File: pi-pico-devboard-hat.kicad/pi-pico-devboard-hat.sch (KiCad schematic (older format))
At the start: 27 parts, among them J1 Conn_01x24_Male, J2 I2C, J3 SDA_UP, J4 SCL_UP, J5 Conn_SPI, J6 Conn_Ext, J7 Conn_BTN, J8 Conn_LED, P1 Conn_02x20_Odd_Even, SW1 SW_Reset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

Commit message: Rev 8: added power-connector / fine-tuning
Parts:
- added J9: Conn_02x03_Odd_Even, Connector_PinHeader_2.54mm:PinHeader_2x03_P2.54mm_Vertical, symbol Connector_Generic:Conn_02x03_Odd_Even
- J5: footprint Connector_PinHeader_2.54mm:PinHeader_1x07_P2.54mm_Vertical -> Connector_PinHeader_2.54mm:PinHeader_1x06_P2.54mm_Vertical; symbol Connector:Conn_01x07_Male -> Connector:Conn_01x06_Male
- J6: footprint Connector_PinHeader_2.54mm:PinHeader_1x04_P2.54mm_Vertical -> Connector_PinHeader_2.54mm:PinHeader_1x03_P2.54mm_Vertical; symbol Connector:Conn_01x04_Male -> Connector:Conn_01x03_Male
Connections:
- net 3V3: now also J9.1 (Pin_1), J9.3 (Pin_3), J9.5 (Pin_5)
- net GND: now also J9.2 (Pin_2), J9.4 (Pin_4), J9.6 (Pin_6)
- net GP8: now reaches U1.11 (GPIO8)
- net GP8: now also J6.3 (Pin_3)
- net SPI_CS_GP13: now reaches U1.17 (GPIO13)
- net SPI_CS_GP13: now also J5.6 (Pin_6)
- no-connect marks 23 -> 21
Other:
- note added: "Power"
- note removed: "SPI1_CS"
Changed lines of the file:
@@
 Title "pi-pico-devboard-hat"
 Date "2021-03-23"
-Rev "7"
+Rev "8"
 Comp "Bernhard Bablok"
 Comment1 "https://github.com/bablokb/pi-pico-devboard-hat"
@@
 NoConn ~ 6500 4200
 NoConn ~ 6500 4300
-NoConn ~ 6500 4400
 NoConn ~ 6500 4500
 NoConn ~ 6500 4700
 NoConn ~ 6500 4800
-NoConn ~ 6500 5000
 NoConn ~ 8700 4000
 NoConn ~ 8700 4200
@@
 Connection ~ 1350 4700
 $Comp
-L Connector:Conn_01x07_Male J5
+L Connector:Conn_01x06_Male J5
 U 1 1 605903A9
-P 950 5650
-F 0 "J5" H 1050 6200 50  0000 C CNN
-F 1 "Conn_SPI" H 1050 6100 50  0000 C CNN
-F 2 "Connector_PinHeader_2.54mm:PinHeader_1x07_P2.54mm_Vertical" H 950 5650 50  0001 C CNN
-F 3 "~" H 950 5650 50  0001 C CNN
-	1    950  5650
+P 950 5550
+F 0 "J5" H 1050 6000 50  0000 C CNN
+F 1 "Conn_SPI" H 1050 5900 50  0000 C CNN
+F 2 "Connector_PinHeader_2.54mm:PinHeader_1x06_P2.54mm_Vertical" H 950 5550 50  0001 C CNN
+F 3 "~" H 950 5550 50  0001 C CNN
+	1    950  5550
 	1    0    0    -1
 $EndComp
@@
 Wire Wire Line
 	1150 5750 1500 5750
-Wire Wire Line
-	1150 5950 1150 5850
-Text Notes 1250 5900 0    50   ~ 0
-SPI1_CS
 Text Label 6500 5300 2    50   ~ 0
 SPI1TX_GP15
@@
 Wire Notes Line
 	2600 3550 750  3550
-Wire Notes Line
-	750  6100 750  5000
 Text Notes 2000 4850 0    50   ~ 0
 I2C-Connector
@@
 SPI-Connector
 Wire Notes Line
-	2600 5000 2600 6100
-Wire Notes Line
 	750  5000 2600 5000
-Wire Notes Line
-	750  6100 2600 6100
-$Comp
-L Connector:Conn_01x04_Male J6
+$Comp
+L Connector:Conn_01x03_Male J6
 U 1 1 605A6142
 P 2850 5450
 F 0 "J6" H 2950 5800 50  0000 C CNN
 F 1 "Conn_Ext" H 2950 5700 50  0000 C CNN
-F 2 "Connector_PinHeader_2.54mm:PinHeader_1x04_P2.54mm_Vertical" H 2850 5450 50  0001 C CNN
+F 2 "Connector_PinHeader_2.54mm:PinHeader_1x03_P2.54mm_Vertical" H 2850 5450 50  0001 C CNN
 F 3 "~" H 2850 5450 50  0001 C CNN
 	1    2850 5450
@@
 Wire Wire Line
 	3050 5450 3700 5450
-Wire Wire Line
-	3050 5650 3050 5550
 Wire Notes Line
 	2750 5000 3800 5000
@@
 Text Notes 9450 2100 0    50   ~ 0
 LEDs
+Text Label 6500 5000 2    50   ~ 0
+SPI_CS_GP13
+Text Label 1500 5850 0    50   ~ 0
+SPI_CS_GP13
+Wire Wire Line
+	1150 5850 1500 5850
+Wire Notes Line
+	2600 5000 2600 6100
+Wire Notes Line
+	2600 6100 750  6100
+Wire Notes Line
+	750  6100 750  5000
+Text Label 6500 4400 2    50   ~ 0
+GP8
+Text Label 3400 5550 0    50   ~ 0
+GP8
+Wire Wire Line
+	3050 5550 3400 5550
+$Comp
+L Connector_Generic:Conn_02x03_Odd_Even J9
+U 1 1 608162C5
+P 3200 4000
+F 0 "J9" H 3250 4317 50  0000 C CNN
+F 1 "Conn_02x03_Odd_Even" H 3250 4226 50  0000 C CNN
+F 2 "Connector_PinHeader_2.54mm:PinHeader_2x03_P2.54mm_Vertical" H 3200 4000 50  0001 C CNN
+F 3 "~" H 3200 4000 50  0001 C CNN
+	1    3200 4000
+	1    0    0    -1
+$EndComp
+$Comp
+L power:GND #PWR011
+U 1 1 60817D38
+P 3500 4450
+F 0 "#PWR011" H 3500 4200 50  0001 C CNN
+F 1 "GND" V 3505 4322 50  0000 R CNN
+F 2 "" H 3500 4450 50  0001 C CNN
+F 3 "" H 3500 4450 50  0001 C CNN
+	1    3500 4450
+	1    0    0    -1
+$EndComp
+Text Label 3000 4500 3    50   ~ 0
+3V3
+Wire Wire Line
+	3000 4500 3000 4100
+Connection ~ 3000 4000
+Wire Wire Line
+	3000 4000 3000 3900
+Connection ~ 3000 4100
+Wire Wire Line
+	3000 4100 3000 4000
+Wire Wire Line
+	3500 4450 3500 4100
+Connection ~ 3500 4000
+Wire Wire Line
+	3500 4000 3500 3900
+Connection ~ 3500 4100
+Wire Wire Line
+	3500 4100 3500 4000
+Wire Notes Line
+	3800 4900 3800 3550
+Text Notes 3500 4850 0    50   ~ 0
+Power
+Wire Notes Line
+	2750 4900 2750 3550
+Wire Notes Line
+	2750 4900 3800 4900
+Wire Notes Line
+	2750 3550 3800 3550
 $EndSCHEMATC

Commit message: Rev 9: added master power-jumper
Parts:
- added J10: Conn_Master_On, Connector_PinHeader_2.54mm:PinHeader_1x02_P2.54mm_Vertical, symbol Connector:Conn_01x02_Male
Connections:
- net +5V: now also J10.2 (Pin_2); no longer D1.2 (A)
- new net: D1.2 (A), J10.1 (Pin_1)
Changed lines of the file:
@@
 Sheet 1 1
 Title "pi-pico-devboard-hat"
-Date "2021-03-23"
-Rev "8"
+Date "2021-03-27"
+Rev "9"
 Comp "Bernhard Bablok"
 Comment1 "https://github.com/bablokb/pi-pico-devboard-hat"
@@
 L power:+5V #PWR06
 U 1 1 6052A522
-P 9800 2800
-F 0 "#PWR06" H 9800 2650 50  0001 C CNN
-F 1 "+5V" H 9800 2940 50  0000 C CNN
-F 2 "" H 9800 2800 50  0000 C CNN
-F 3 "" H 9800 2800 50  0000 C CNN
-	1    9800 2800
+P 9800 2600
+F 0 "#PWR06" H 9800 2450 50  0001 C CNN
+F 1 "+5V" H 9800 2740 50  0000 C CNN
+F 2 "" H 9800 2600 50  0000 C CNN
+F 3 "" H 9800 2600 50  0000 C CNN
+	1    9800 2600
 	1    0    0    -1
 $EndComp
@@
 	0    -1   -1   0
 $EndComp
-$Comp
-L power:PWR_FLAG #FLG0101
-U 1 1 605568F4
-P 9800 2800
-F 0 "#FLG0101" H 9800 2875 50  0001 C CNN
-F 1 "PWR_FLAG" V 9800 2928 50  0000 L CNN
-F 2 "" H 9800 2800 50  0001 C CNN
-F 3 "~" H 9800 2800 50  0001 C CNN
-	1    9800 2800
-	0    1    1    0
-$EndComp
-Connection ~ 9800 2800
 Wire Wire Line
 	7600 5650 9800 5650
@@
 Wire Notes Line
 	2750 3550 3800 3550
+$Comp
+L Connector:Conn_01x02_Male J10
+U 1 1 605FB177
+P 10000 2700
+F 0 "J10" H 9972 2582 50  0000 R CNN
+F 1 "Conn_Master_On" H 9972 2673 50  0000 R CNN
+F 2 "Connector_PinHeader_2.54mm:PinHeader_1x02_P2.54mm_Vertical" H 10000 2700 50  0001 C CNN
+F 3 "~" H 10000 2700 50  0001 C CNN
+	1    10000 2700
+	-1   0    0    1
+$EndComp
+Wire Wire Line
+	9800 2700 9800 2800
+$Comp
+L power:PWR_FLAG #FLG0110
+U 1 1 60612B48
+P 3100 950
+F 0 "#FLG0110" H 3100 1025 50  0001 C CNN
+F 1 "PWR_FLAG" V 3100 1078 50  0000 L CNN
+F 2 "" H 3100 950 50  0001 C CNN
+F 3 "~" H 3100 950 50  0001 C CNN
+	1    3100 950
+	0    1    1    0
+$EndComp
+Connection ~ 3100 950
 $EndSCHEMATC

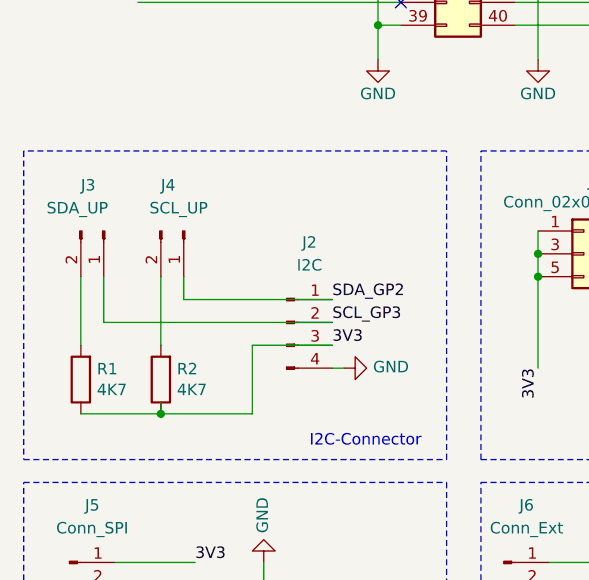
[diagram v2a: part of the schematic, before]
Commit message: Rev 10: reorg of I2C-pullup connector
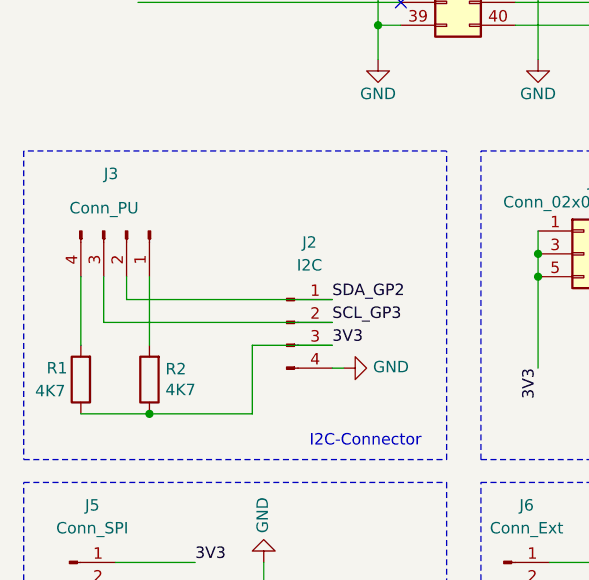
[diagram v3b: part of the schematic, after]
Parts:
- removed J3: SDA_UP, Connector_PinHeader_2.54mm:PinHeader_1x02_P2.54mm_Vertical, symbol Connector:Conn_01x02_Male
- removed J4: SCL_UP, Connector_PinHeader_2.54mm:PinHeader_1x02_P2.54mm_Vertical, symbol Connector:Conn_01x02_Male
- added J3: Conn_PU, Connector_PinHeader_2.54mm:PinHeader_1x04_P2.54mm_Vertical, symbol Connector:Conn_01x04_Male
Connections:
- net SCL_GP3: now also J3.3 (Pin_3)
- net SDA_GP2: now also J3.2 (Pin_2)
- net at R2.2: now also J3.1 (Pin_1)
- net at R1.2: now also J3.4 (Pin_4)
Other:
- moved on the sheet: R2
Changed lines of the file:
@@
 Title "pi-pico-devboard-hat"
 Date "2021-03-27"
-Rev "9"
+Rev "10"
 Comp "Bernhard Bablok"
 Comment1 "https://github.com/bablokb/pi-pico-devboard-hat"
@@
 L Device:R R2
 U 1 1 6062584D
-P 1350 4550
-F 0 "R2" H 1280 4504 50  0000 R CNN
-F 1 "4K7" H 1280 4595 50  0000 R CNN
-F 2 "Resistor_THT:R_Axial_DIN0204_L3.6mm_D1.6mm_P5.08mm_Horizontal" V 1280 4550 50  0001 C CNN
-F 3 "~" H 1350 4550 50  0001 C CNN
-	1    1350 4550
+P 1300 4550
+F 0 "R2" H 1230 4504 50  0000 R CNN
+F 1 "4K7" H 1230 4595 50  0000 R CNN
+F 2 "Resistor_THT:R_Axial_DIN0204_L3.6mm_D1.6mm_P5.08mm_Horizontal" V 1230 4550 50  0001 C CNN
+F 3 "~" H 1300 4550 50  0001 C CNN
+	1    1300 4550
 	-1   0    0    1
 $EndComp
@@
 U 1 1 60626297
 P 1000 4550
-F 0 "R1" H 930 4504 50  0000 R CNN
-F 1 "4K7" H 930 4595 50  0000 R CNN
+F 0 "R1" H 1150 4500 50  0000 R CNN
+F 1 "4K7" H 1200 4600 50  0000 R CNN
 F 2 "Resistor_THT:R_Axial_DIN0204_L3.6mm_D1.6mm_P5.08mm_Horizontal" V 930 4550 50  0001 C CNN
 F 3 "~" H 1000 4550 50  0001 C CNN
@@
 	-1   0    0    1
 $EndComp
-$Comp
-L Connector:Conn_01x02_Male J3
-U 1 1 60626EA3
-P 1100 3900
-F 0 "J3" V 900 3800 50  0000 L CNN
-F 1 "SDA_UP" V 1000 3650 50  0000 L CNN
-F 2 "Connector_PinHeader_2.54mm:PinHeader_1x02_P2.54mm_Vertical" H 1100 3900 50  0001 C CNN
-F 3 "~" H 1100 3900 50  0001 C CNN
-	1    1100 3900
-	0    1    1    0
-$EndComp
-$Comp
-L Connector:Conn_01x02_Male J4
-U 1 1 606291D7
-P 1450 3900
-F 0 "J4" V 1250 3800 50  0000 L CNN
-F 1 "SCL_UP" V 1350 3750 50  0000 L CNN
-F 2 "Connector_PinHeader_2.54mm:PinHeader_1x02_P2.54mm_Vertical" H 1450 3900 50  0001 C CNN
-F 3 "~" H 1450 3900 50  0001 C CNN
-	1    1450 3900
-	0    1    1    0
-$EndComp
-Wire Wire Line
-	2100 4200 1450 4200
-Wire Wire Line
-	1450 4200 1450 4100
 Wire Wire Line
 	2100 4300 1100 4300
@@
 	1000 4100 1000 4400
 Wire Wire Line
-	1350 4100 1350 4400
-Wire Wire Line
 	2100 4400 1750 4400
 Wire Wire Line
 	1750 4400 1750 4700
-Wire Wire Line
-	1750 4700 1350 4700
-Wire Wire Line
-	1350 4650 1350 4700
-Wire Wire Line
-	1350 4700 1000 4700
-Connection ~ 1350 4700
 $Comp
 L Connector:Conn_01x06_Male J5
@@
 $EndComp
 Connection ~ 3100 950
+$Comp
+L Connector:Conn_01x04_Male J3
+U 1 1 606247ED
+P 1200 3900
+F 0 "J3" V 950 3800 50  0000 L CNN
+F 1 "Conn_PU" V 1100 3650 50  0000 L CNN
+F 2 "Connector_PinHeader_2.54mm:PinHeader_1x04_P2.54mm_Vertical" H 1200 3900 50  0001 C CNN
+F 3 "~" H 1200 3900 50  0001 C CNN
+	1    1200 3900
+	0    1    1    0
+$EndComp
+Wire Wire Line
+	1200 4200 1200 4100
+Wire Wire Line
+	1200 4200 2100 4200
+Connection ~ 1300 4700
+Wire Wire Line
+	1300 4700 1750 4700
+Wire Wire Line
+	1300 4400 1300 4100
+Wire Wire Line
+	1000 4700 1300 4700
 $EndSCHEMATC

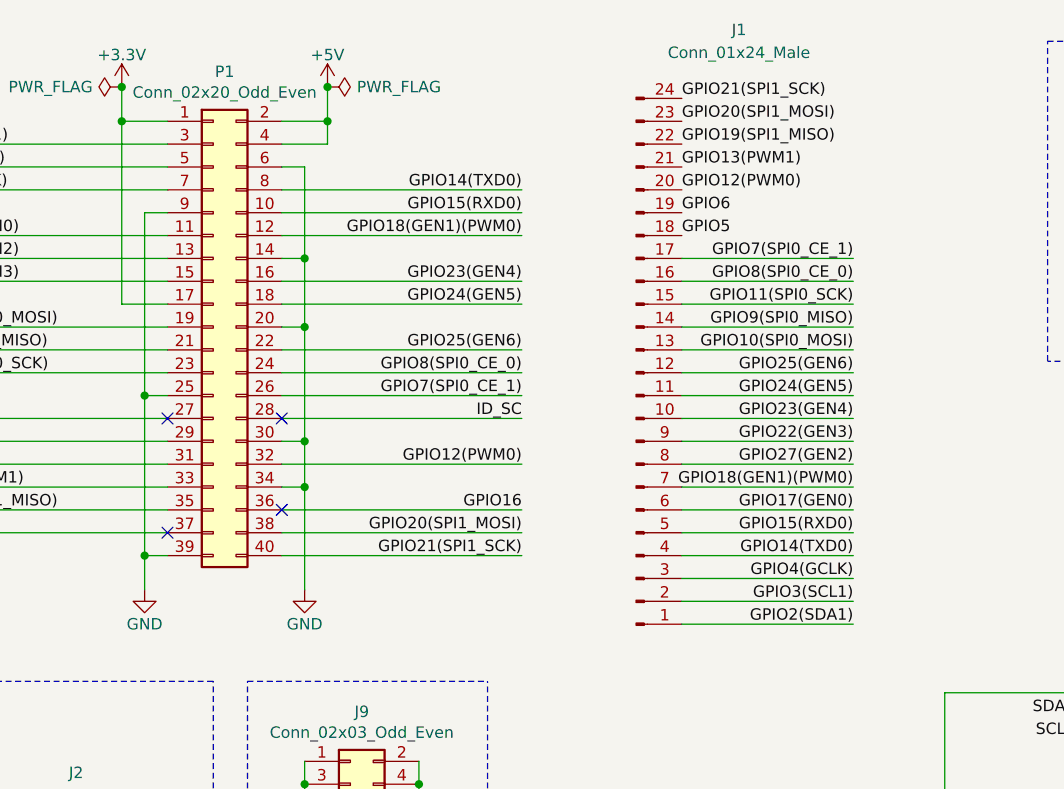
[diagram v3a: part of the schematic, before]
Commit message: Rev 11: connect Pi-pins GPIO16/GPIO26 to pin-connector (remove GPIO24/GPIO25 used for SWD)
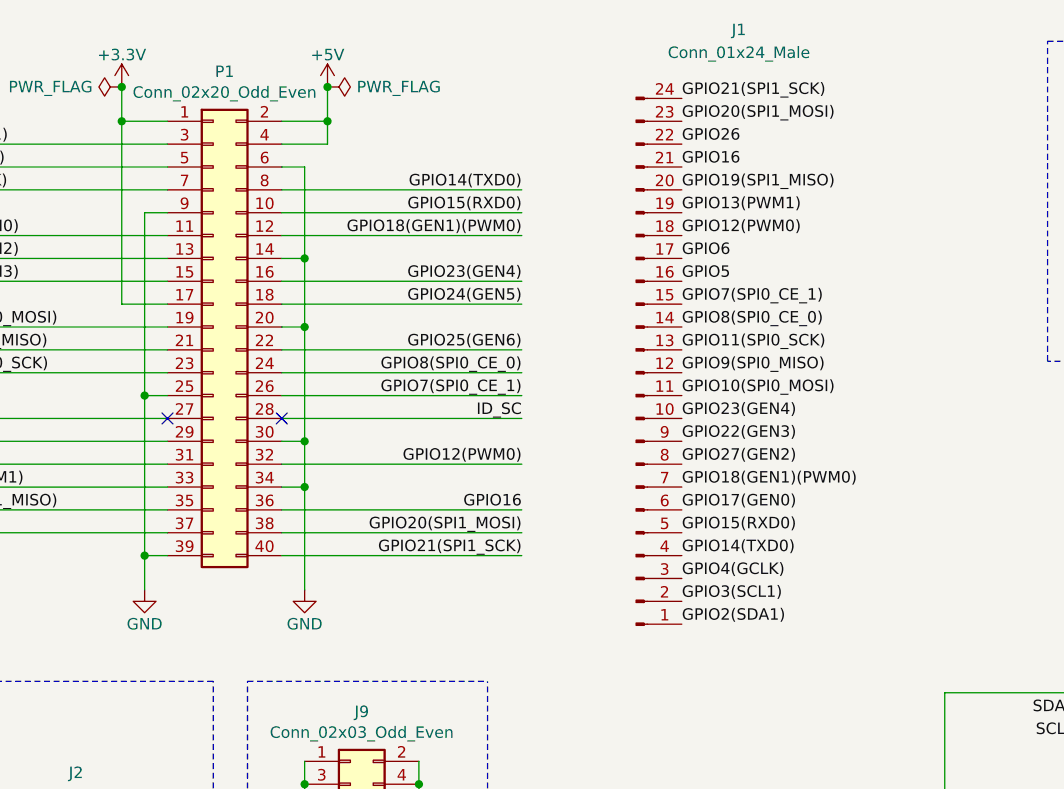
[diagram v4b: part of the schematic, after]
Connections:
- net GPIO10(SPI0_MOSI): now also J1.11 (Pin_11); no longer J1.13 (Pin_13)
- net GPIO11(SPI0_SCK): now also J1.13 (Pin_13); no longer J1.15 (Pin_15)
- net GPIO12(PWM0): now also J1.18 (Pin_18); no longer J1.20 (Pin_20)
- net GPIO13(PWM1): now also J1.19 (Pin_19); no longer J1.21 (Pin_21)
- net GPIO16: now also J1.21 (Pin_21)
- net GPIO19(SPI1_MISO): now also J1.20 (Pin_20); no longer J1.22 (Pin_22)
- net GPIO24(GEN5): no longer J1.11 (Pin_11)
- net GPIO25(GEN6): no longer J1.12 (Pin_12)
- net GPIO26: now also J1.22 (Pin_22)
- net GPIO5: now also J1.16 (Pin_16); no longer J1.18 (Pin_18)
- net GPIO6: now also J1.17 (Pin_17); no longer J1.19 (Pin_19)
- net GPIO7(SPI0_CE_1): now also J1.15 (Pin_15); no longer J1.17 (Pin_17)
- net GPIO8(SPI0_CE_0): now also J1.14 (Pin_14); no longer J1.16 (Pin_16)
- net GPIO9(SPI0_MISO): now also J1.12 (Pin_12); no longer J1.14 (Pin_14)
- no-connect marks 21 -> 19
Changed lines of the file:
@@
 Title "pi-pico-devboard-hat"
 Date "2021-03-27"
-Rev "10"
+Rev "11"
 Comp "Bernhard Bablok"
 Comment1 "https://github.com/bablokb/pi-pico-devboard-hat"
@@
 	1    0    0    1
 $EndComp
-Wire Wire Line
-	4650 3300 5400 3300
-Wire Wire Line
-	4650 3200 5400 3200
-Text Label 5400 3300 2    50   ~ 0
-GPIO2(SDA1)
-Text Label 5400 3200 2    50   ~ 0
-GPIO3(SCL1)
-Wire Wire Line
-	4650 3100 5400 3100
-Wire Wire Line
-	4650 3000 5400 3000
-Wire Wire Line
-	4650 2900 5400 2900
-Wire Wire Line
-	4650 2800 5400 2800
-Wire Wire Line
-	4650 2700 5400 2700
-Wire Wire Line
-	4650 2600 5400 2600
-Wire Wire Line
-	4650 2500 5400 2500
-Wire Wire Line
-	4650 2400 5400 2400
-Wire Wire Line
-	4650 2300 5400 2300
-Wire Wire Line
-	4650 2200 5400 2200
-Wire Wire Line
-	4650 2100 5400 2100
-Wire Wire Line
-	4650 2000 5400 2000
-Wire Wire Line
-	4650 1900 5400 1900
-Wire Wire Line
-	4650 1800 5400 1800
-Wire Wire Line
-	4650 1700 5400 1700
-Text Label 5400 3100 2    50   ~ 0
-GPIO4(GCLK)
-Text Label 5400 3000 2    50   ~ 0
-GPIO14(TXD0)
-Text Label 5400 2900 2    50   ~ 0
-GPIO15(RXD0)
-Text Label 5400 2800 2    50   ~ 0
-GPIO17(GEN0)
-Text Label 5400 2700 2    50   ~ 0
-GPIO18(GEN1)(PWM0)
-Text Label 5400 2600 2    50   ~ 0
-GPIO27(GEN2)
-Text Label 5400 2500 2    50   ~ 0
-GPIO22(GEN3)
-Text Label 5400 2400 2    50   ~ 0
-GPIO23(GEN4)
-Text Label 5400 2300 2    50   ~ 0
-GPIO24(GEN5)
-Text Label 5400 2200 2    50   ~ 0
-GPIO25(GEN6)
-Text Label 5400 2100 2    50   ~ 0
-GPIO10(SPI0_MOSI)
-Text Label 5400 2000 2    50   ~ 0
-GPIO9(SPI0_MISO)
-Text Label 5400 1900 2    50   ~ 0
-GPIO11(SPI0_SCK)
-Text Label 5400 1800 2    50   ~ 0
-GPIO8(SPI0_CE_0)
-Text Label 5400 1700 2    50   ~ 0
+Text Label 4650 1900 0    50   ~ 0
 GPIO7(SPI0_CE_1)
-Text Label 4650 1200 0    50   ~ 0
+Text Label 4650 1400 0    50   ~ 0
 GPIO19(SPI1_MISO)
+Text Label 4650 1800 0    50   ~ 0
+GPIO5
+Text Label 4650 1700 0    50   ~ 0
+GPIO6
 Text Label 4650 1600 0    50   ~ 0
-GPIO5
+GPIO12(PWM0)
 Text Label 4650 1500 0    50   ~ 0
-GPIO6
-Text Label 4650 1400 0    50   ~ 0
-GPIO12(PWM0)
-Text Label 4650 1300 0    50   ~ 0
 GPIO13(PWM1)
 Text Label 4650 1100 0    50   ~ 0
@@
 NoConn ~ 2400 2400
 NoConn ~ 2900 2400
-NoConn ~ 2900 2800
-NoConn ~ 2400 2900
 Wire Wire Line
 	9800 4600 10050 4600
@@
 Wire Wire Line
 	1000 4700 1300 4700
+Text Label 4650 1300 0    50   ~ 0
+GPIO16
+Text Label 4650 1200 0    50   ~ 0
+GPIO26
+Text Label 4650 2000 0    50   ~ 0
+GPIO8(SPI0_CE_0)
+Text Label 4650 2100 0    50   ~ 0
+GPIO11(SPI0_SCK)
+Text Label 4650 2200 0    50   ~ 0
+GPIO9(SPI0_MISO)
+Text Label 4650 2300 0    50   ~ 0
+GPIO10(SPI0_MOSI)
+Text Label 4650 2400 0    50   ~ 0
+GPIO23(GEN4)
+Text Label 4650 2500 0    50   ~ 0
+GPIO22(GEN3)
+Text Label 4650 2600 0    50   ~ 0
+GPIO27(GEN2)
+Text Label 4650 2700 0    50   ~ 0
+GPIO18(GEN1)(PWM0)
+Text Label 4650 2800 0    50   ~ 0
+GPIO17(GEN0)
+Text Label 4650 2900 0    50   ~ 0
+GPIO15(RXD0)
+Text Label 4650 3000 0    50   ~ 0
+GPIO14(TXD0)
+Text Label 4650 3100 0    50   ~ 0
+GPIO4(GCLK)
+Text Label 4650 3200 0    50   ~ 0
+GPIO3(SCL1)
+Text Label 4650 3300 0    50   ~ 0
+GPIO2(SDA1)
 $EndSCHEMATC
